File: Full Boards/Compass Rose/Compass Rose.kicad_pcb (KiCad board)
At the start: 4 copper layers, 170 x 180 mm, 252 parts, among them J1 Program Header, J3 Optional Bond, Q1 BSS314PE, Q2 DMN6075S, Q3 BSS314PE, Q4 DMN6075S, Q5 BSS314PE, Q6 DMN6075S, SW1 Boot, SW2 Reset, SW3 CTS_219-2MSTR

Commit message: Finished layout of the battery display PCB. Updated the silkscreen on the Compass Rose as well.
Signed-off-by: digimer <digital.mermaid@gmail.com>
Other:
- board text added: "0x55"
- board text added: "0x57"
- board text added: "I2C Addr: 0x28"
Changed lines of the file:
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@@
 		(layer "Edge.Cuts")
+	)
+	(gr_text "I2C Addr: 0x28"
+		(at 209.5 120.6 0)
+		(layer "F.SilkS")
+		(effects
+			(font
+				(size 1 1)
+				(thickness 0.125)
+			)
+			(justify left bottom)
+		)
 	)
 	(gr_text "2-Ring Compass Rose\nv4.1 - Prototype - 01\n© The Digital Mermaid - 2026"
@@
 		)
 	)
+	(gr_text "0x55"
+		(at 140.8 106.7 90)
+		(layer "F.SilkS")
+		(effects
+			(font
+				(size 1 1)
+				(thickness 0.15)
+			)
+			(justify left bottom)
+		)
+	)
+	(gr_text "0x57"
+		(at 140.8 113 90)
+		(layer "F.SilkS")
+		(effects
+			(font
+				(size 1 1)
+				(thickness 0.15)
+			)
+			(justify left bottom)
+		)
+	)

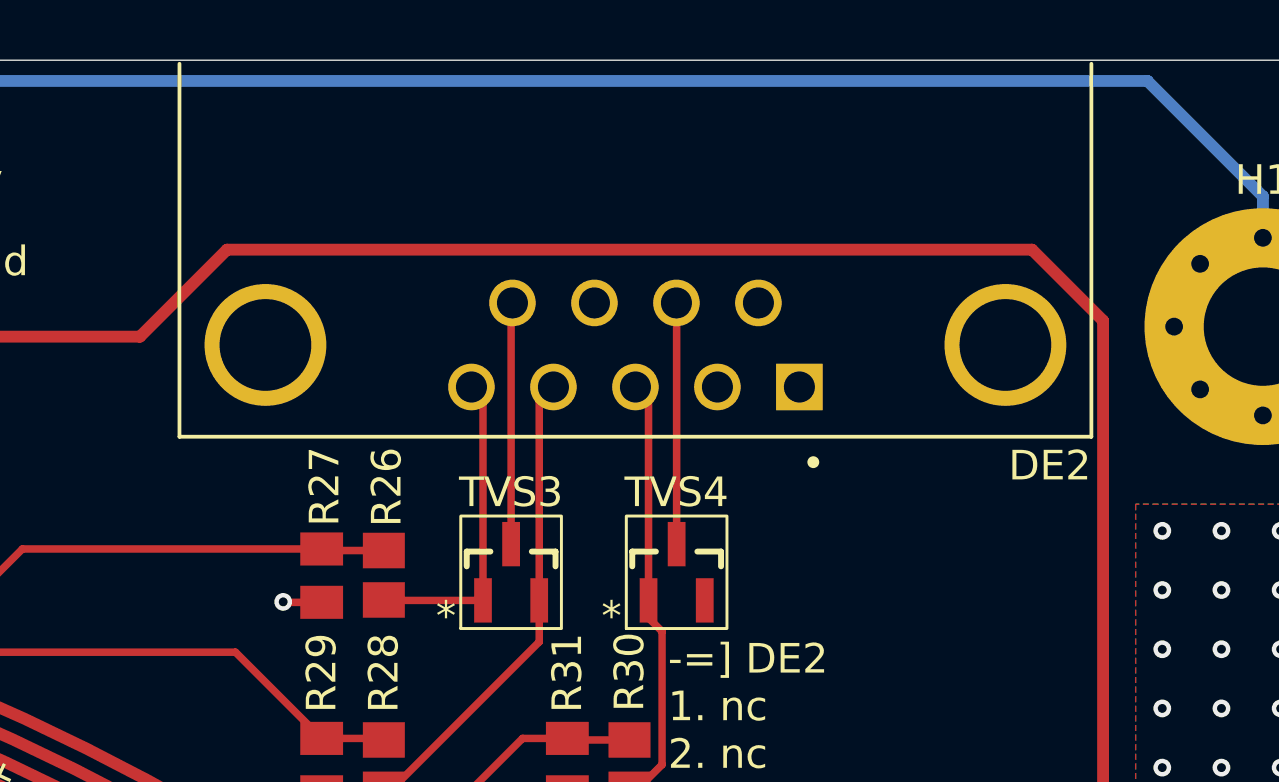
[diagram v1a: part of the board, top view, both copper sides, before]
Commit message: Upated Compass Rose schematic and PCB to match the updated DE and LED footprints.
Signed-off-by: digimer <digital.mermaid@gmail.com>
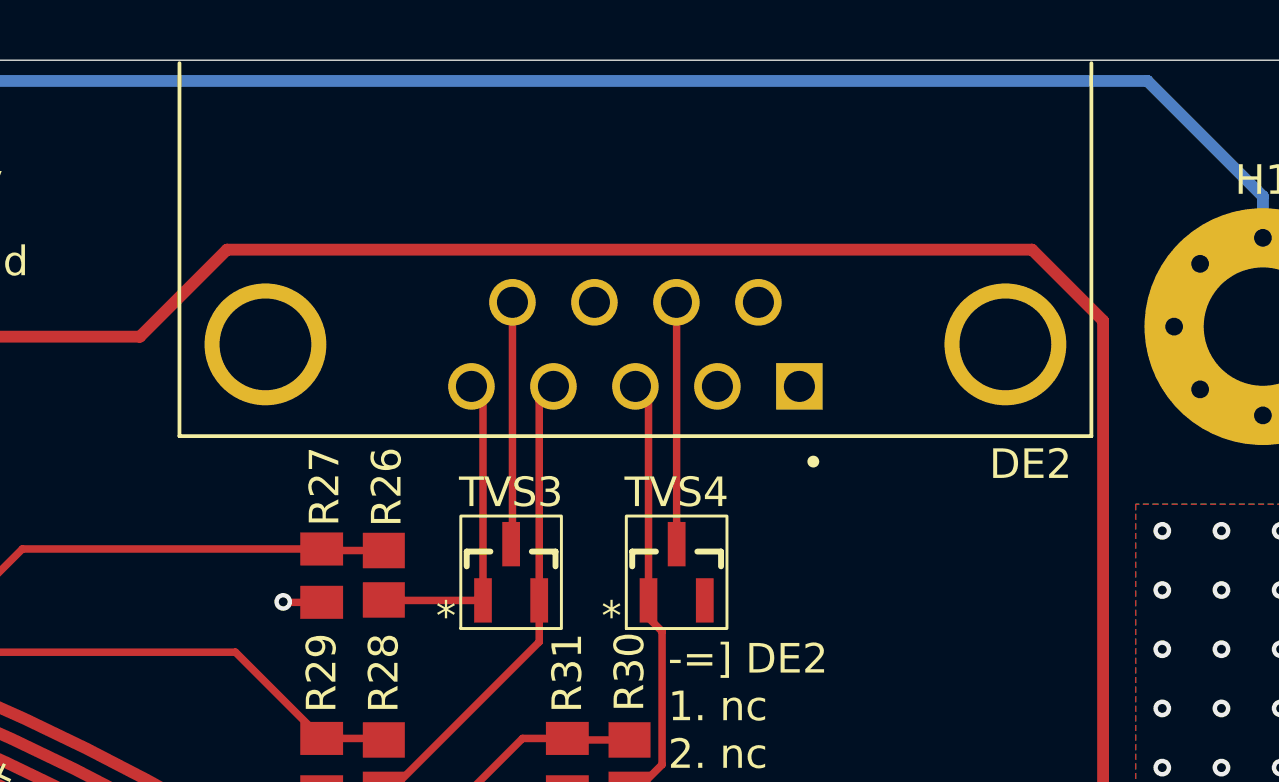
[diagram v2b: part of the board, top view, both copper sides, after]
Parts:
- DE2: footprint mr-stuff:Amphenol_L777SDE09PA4CH4F -> mr-stuff:Amphenol L777SDE09PA4CH4F
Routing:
- net /DISPLAY_ON_IN_PLUG: track 13.3 -> 13.9 mm
- net /LCD_PGUP_IN_PLUG: track 10.2 -> 10.7 mm
